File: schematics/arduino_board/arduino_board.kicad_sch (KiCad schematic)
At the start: 4 parts, among them J1 DIN-5_180degree

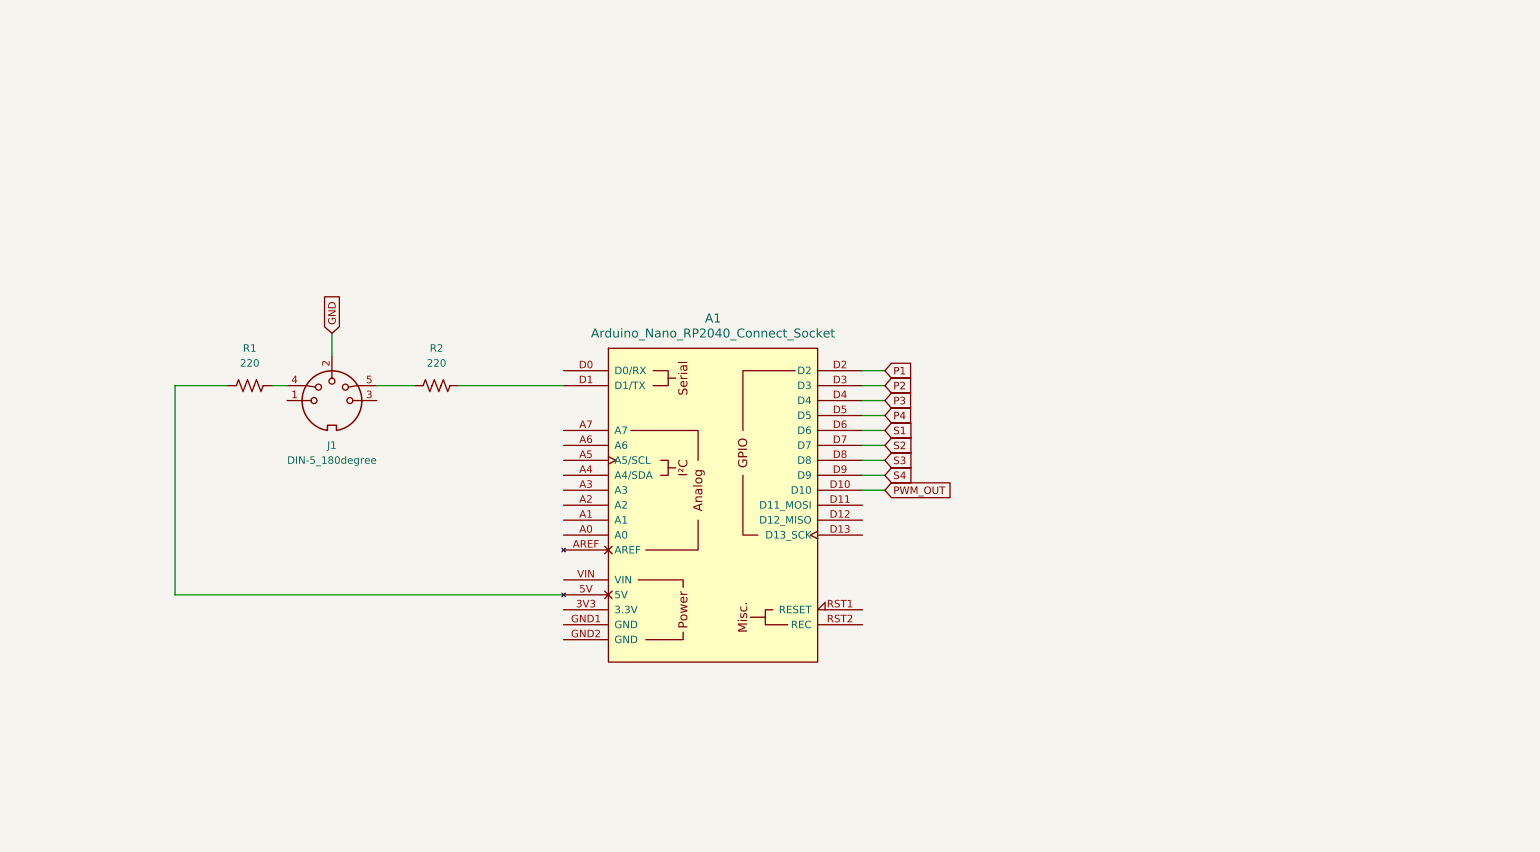
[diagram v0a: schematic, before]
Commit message: schematics updated
added schematics for the front board.
modified arduino board to allow for the use of a nano rp2040 and two rp4922 as DACs for the LFOs and future expansion
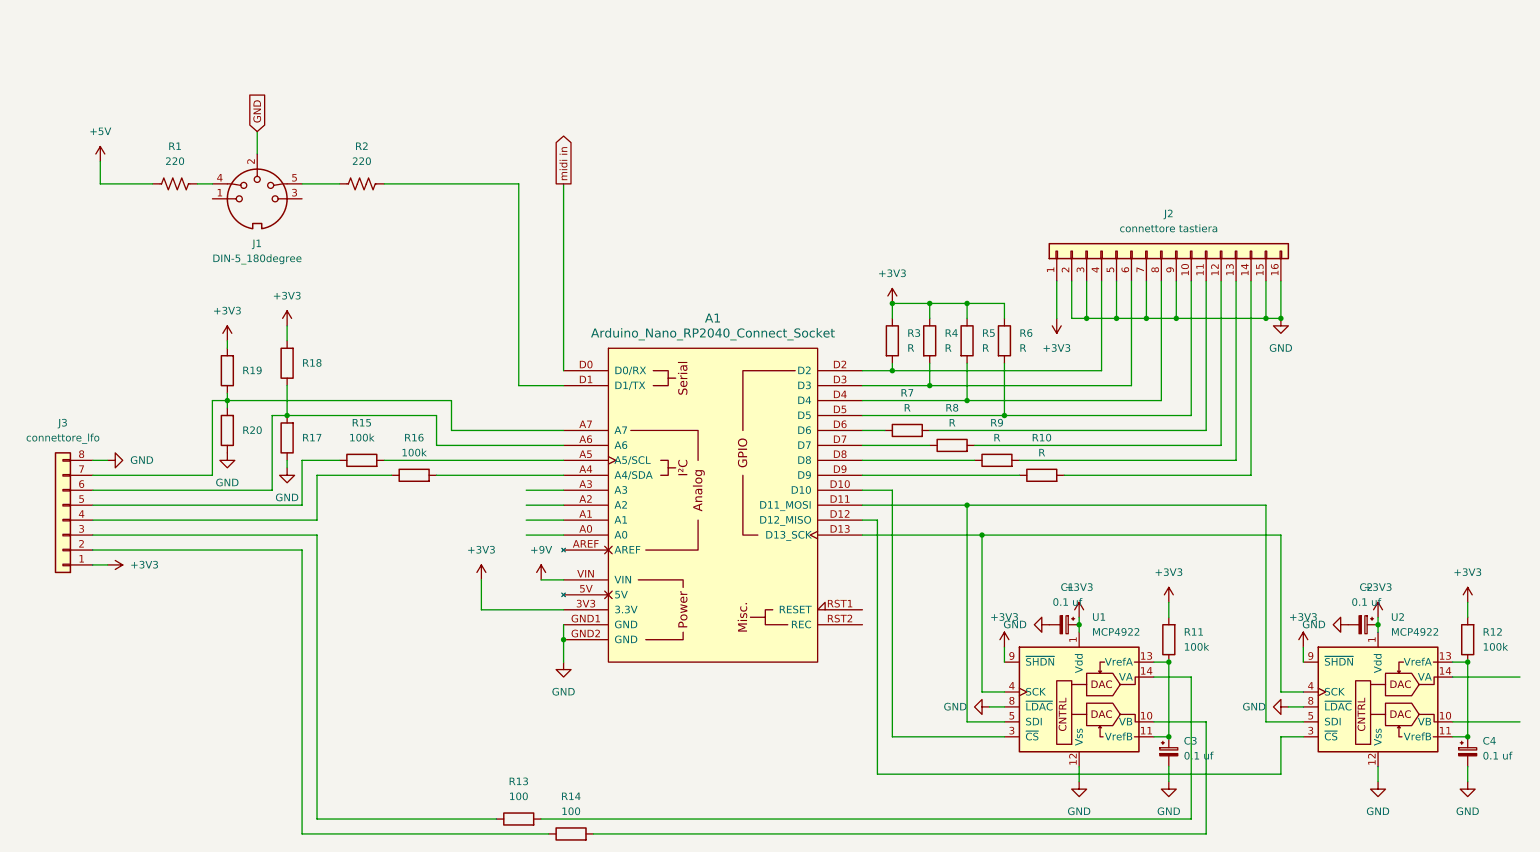
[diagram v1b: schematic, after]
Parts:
- added C1, C2, C3, C4: 0.1 uf, symbol Device:C_Polarized_Small
- added J2: connettore tastiera, symbol Connector_Generic:Conn_01x16
- added J3: connettore_lfo, symbol Connector_Generic:Conn_01x08
- added R10, R3, R4, R5, R6, R7, R8, R9: R, symbol Device:R
- added R11, R12, R15, R16: 100k, symbol Device:R
- added R13, R14: 100, symbol Device:R
- added R17, R18, R19, R20: ~, symbol Device:R
- added U1, U2: MCP4922, symbol Analog_DAC:MCP4922
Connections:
- net GND: now also A1.GND1 (GND), A1.GND2 (GND), C1.2, C2.2, C3.2, C4.2, J2.15 (Pin_15), J2.16 (Pin_16), J2.2 (Pin_2), J2.3 (Pin_3), J2.5 (Pin_5), J2.7 (Pin_7), J2.9 (Pin_9), J3.8 (Pin_8), R17.1, R20.1, U1.12 (Vss), U1.8 (~{LDAC}), U2.12 (Vss), U2.8 (~{LDAC})
- net at A1.5V: no longer R1.1
- net +3V3: now reaches A1.3V3 (3.3V)
- net +3V3: now also C1.1, C2.1, J2.1 (Pin_1), J3.1 (Pin_1), R11.2, R12.2, R18.2, R19.2, R3.1, R4.1, R5.1, R6.1, U1.1 (Vdd), U1.9 (~{SHDN}), U2.1 (Vdd), U2.9 (~{SHDN})
- net at A1.A4 (A4/SDA): now also R16.2
- net at A1.A5 (A5/SCL): now also R15.2
- net at A1.A6: now also J3.6 (Pin_6), R17.2, R18.1
- net at A1.A7: now also J3.7 (Pin_7), R19.1, R20.2
- net midi in: now reaches A1.D0 (D0/RX)
- net at A1.D11 (D11_MOSI): now also U1.5 (SDI), U2.5 (SDI)
- net at A1.D12 (D12_MISO): now also U2.3 (~{CS})
- net at A1.D13 (D13_SCK): now also U1.4 (SCK), U2.4 (SCK)
- net +9V: now reaches A1.VIN
- net P1: no longer names the net of A1.D2
- net P1: now also J2.4 (Pin_4), R3.2
- net P2: no longer names the net of A1.D3
- net P2: now also J2.6 (Pin_6), R4.2
- net P3: no longer names the net of A1.D4
- net P3: now also J2.8 (Pin_8), R5.2
- net P4: no longer names the net of A1.D5
- net P4: now also J2.10 (Pin_10), R6.2
- net PWM_OUT: no longer names the net of A1.D10
- net PWM_OUT: now also U1.3 (~{CS})
- net S1: no longer names the net of A1.D6
- net S1: now also R7.1
- net S2: no longer names the net of A1.D7
- net S2: now also R8.1
- net S3: no longer names the net of A1.D8
- net S3: now also R9.1
- net S4: no longer names the net of A1.D9
- net S4: now also R10.1
- new net: R14.2, U1.10 (VB)
- new net: C3.1, R11.1, U1.11 (VrefB), U1.13 (VrefA)
- new net: R13.2, U1.14 (VA)
- new net: J3.4 (Pin_4), R16.1
- new net: J2.11 (Pin_11), R7.2
- new net: J2.13 (Pin_13), R9.2
- new net: J2.12 (Pin_12), R8.2
- new net: J3.2 (Pin_2), R14.1
- new net: J2.14 (Pin_14), R10.2
- new net: C4.1, R12.1, U2.11 (VrefB), U2.13 (VrefA)
- new net: J3.5 (Pin_5), R15.1
- new net: J3.3 (Pin_3), R13.1
- new net +5V: R1.1
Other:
- moved on the sheet: J1, R1, R2

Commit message: Update arduino_board.kicad_sch
updated resistor values and added midi in
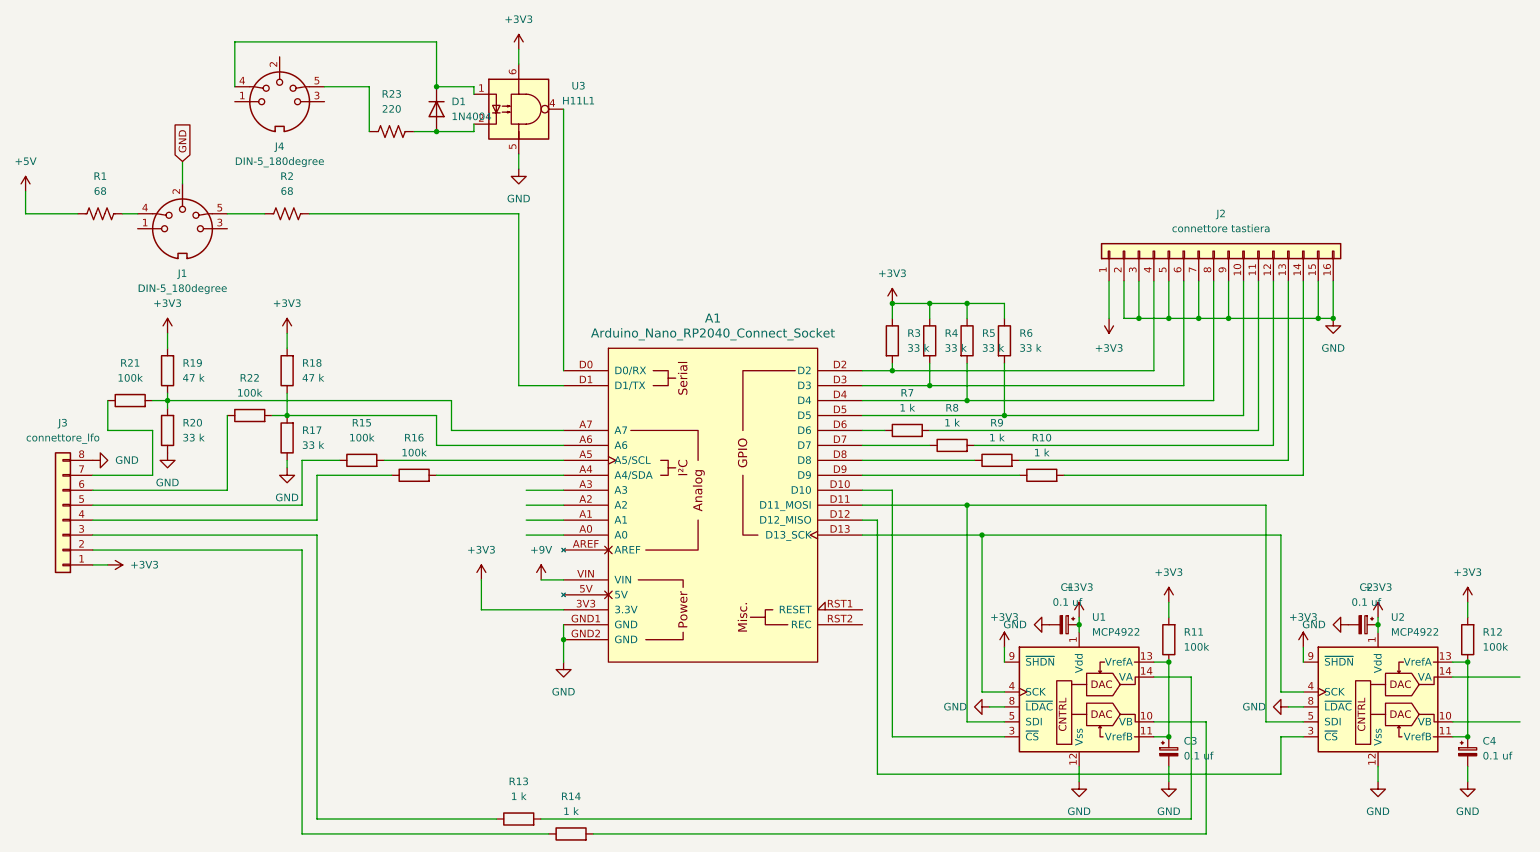
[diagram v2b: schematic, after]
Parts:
- added D1: 1N4004, Diode_THT:D_DO-41_SOD81_P10.16mm_Horizontal, symbol Diode:1N4004
- added J4: DIN-5_180degree, symbol Connector:DIN-5_180degree
- added R21, R22: 100k, symbol Device:R
- added R23: 220, symbol Device:R_US
- added U3: H11L1, symbol Isolator:H11L1
- R1, R2: value 220 -> 68
- R10, R7, R8, R9: value R -> 1 k
- R13, R14: value 100 -> 1 k
- R17, R20: value ~ -> 33 k
- R18, R19: value ~ -> 47 k
- R3, R4, R5, R6: value R -> 33 k
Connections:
- net +3V3: now also U3.6
- net GND: now also U3.5
- net at A1.A7, R19.1, R20.2: now also R21.2; no longer J3.7 (Pin_7)
- net at A1.A6, R17.2, R18.1: now also R22.2; no longer J3.6 (Pin_6)
- net midi in: no longer names the net of A1.D0 (D0/RX)
- net midi in: now also U3.4
- new net: D1.1 (K), J4.4, U3.1
- new net: D1.2 (A), R23.2, U3.2
- new net: J3.7 (Pin_7), R21.1
- new net: J3.6 (Pin_6), R22.1
- new net: J4.5, R23.1
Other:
- moved on the sheet: J1, J2, R1, R18, R19, R2, R20
